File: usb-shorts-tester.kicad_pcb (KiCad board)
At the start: 2 copper layers, 21 x 51 mm, 7 parts, among them J1 CX60-24S-UNIT, J2 USB4080-03-A_REVA1, U1 TCA6424ARGJR

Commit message: Beta release
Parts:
- added C1: 0.1uF, Capacitor_SMD:C_0603_1608Metric, F.Cu at (50.3, 49.4)
- added JP1: I2C0_I2C1_SDA_JMP_Bridged_12, Jumper:SolderJumper-3_P1.3mm_Bridged12_RoundedPad1.0x1.5mm, F.Cu at (48.6, 55.9)
- added JP2: I2C0_I2C1_SCL_JMP_Bridged_12, Jumper:SolderJumper-3_P1.3mm_Bridged12_RoundedPad1.0x1.5mm, F.Cu at (43.6, 55.9)
- added JP5: JMP_ADDR, Jumper:SolderJumper-2_P1.3mm_Open_RoundedPad1.0x1.5mm, F.Cu at (41.0, 50.2)
- added JP6: I2C_PULLUP_JMP_CLOSED, Jumper:SolderJumper-3_P1.3mm_Bridged12_RoundedPad1.0x1.5mm, F.Cu at (46.1, 53.2)
- added R1: 4k7, Resistor_SMD:R_0603_1608Metric, F.Cu at (42.3, 53.7)
- added R2: 4k7, Resistor_SMD:R_0603_1608Metric, F.Cu at (50.0, 53.7)
- added R3: 10k, Resistor_SMD:R_0603_1608Metric, F.Cu at (43.1, 49.2)
- added R4: 10k, Resistor_SMD:R_0603_1608Metric, F.Cu at (48.5, 49.3)
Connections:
- A1 pad 10: unconnected-(A1-GPIO7-Pad10) -> GPIO7
- A1 pad 26: unconnected-(A1-GPIO20-Pad26) -> GPIO20
- A1 pad 27: unconnected-(A1-GPIO21-Pad27) -> GPIO21
- A1 pad 9: unconnected-(A1-GPIO6-Pad9) -> GPIO6
- U1 pad 26: unconnected-(U1-ADDR-Pad26) -> ADDR
- U1 pad 29: unconnected-(U1-SCL-Pad29) -> SCL
- U1 pad 30: unconnected-(U1-SDA-Pad30) -> SDA
- U1 pad 32: unconnected-(U1-~{INT}-Pad32) -> Net-(U1-~{INT})
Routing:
- net GPIO6: track 0.00 -> 29.3 mm, vias 0 -> 2
- net GPIO7: track 0.00 -> 16.9 mm, vias 0 -> 2
- net GND: track 1.91 -> 17.5 mm, vias 0 -> 1
- net GPIO21: track 0.00 -> 14.4 mm, vias 0 -> 1
- net +3V3: track 36.2 -> 50.3 mm, vias 2 -> 5
- net SDA: track 0.00 -> 14.0 mm
- net SCL: track 0.00 -> 12.8 mm
- net RESET: track 11.5 -> 20.2 mm, vias 0 -> 3
- net ADDR: track 0.00 -> 6.15 mm
- net GPIO20: track 0.00 -> 4.86 mm
- net Net-(JP6-B): track 0.00 -> 1.98 mm
- net Net-(JP6-A): track 0.00 -> 1.96 mm
- net Net-(U1-~{INT}): track 0.00 -> 1.86 mm
- net A12: track 46.7 -> 48.2 mm
- net A10: track 46.7 -> 48.0 mm
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
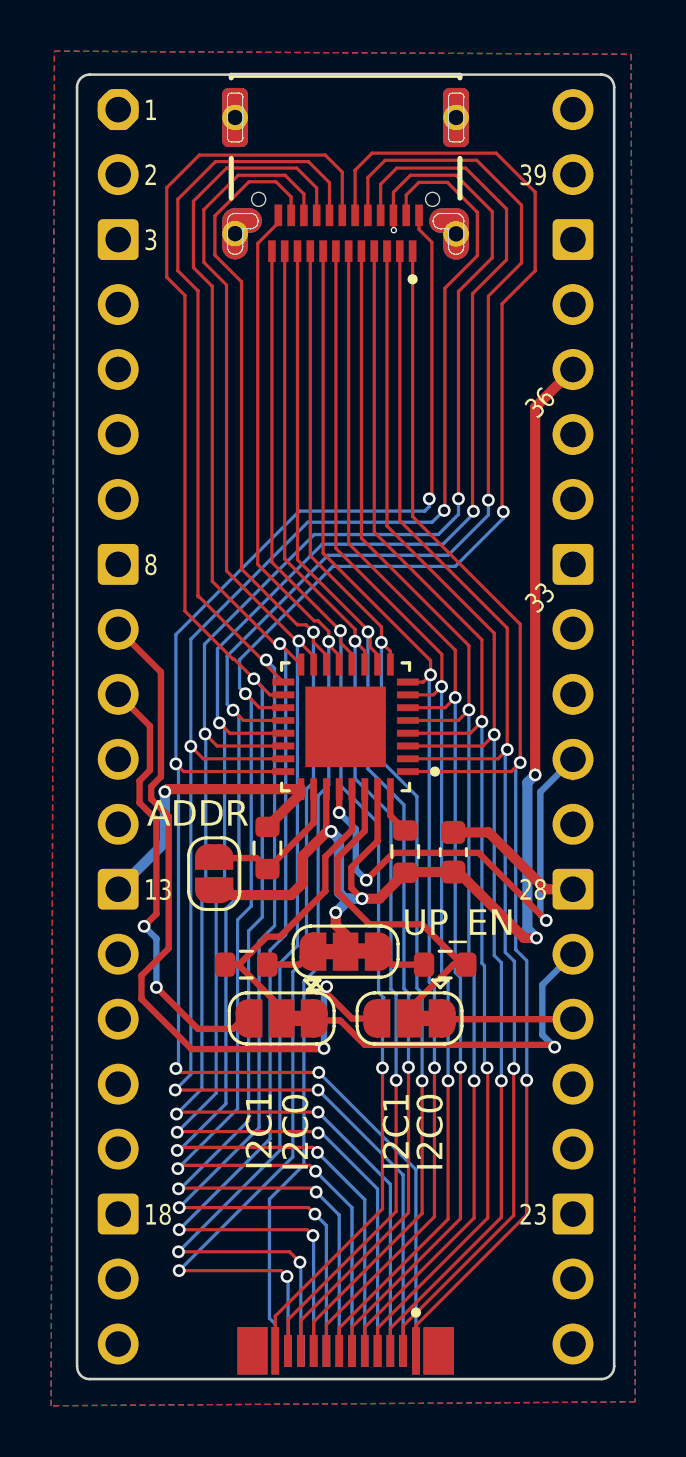
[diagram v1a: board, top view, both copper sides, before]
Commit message: Add usb shield probing
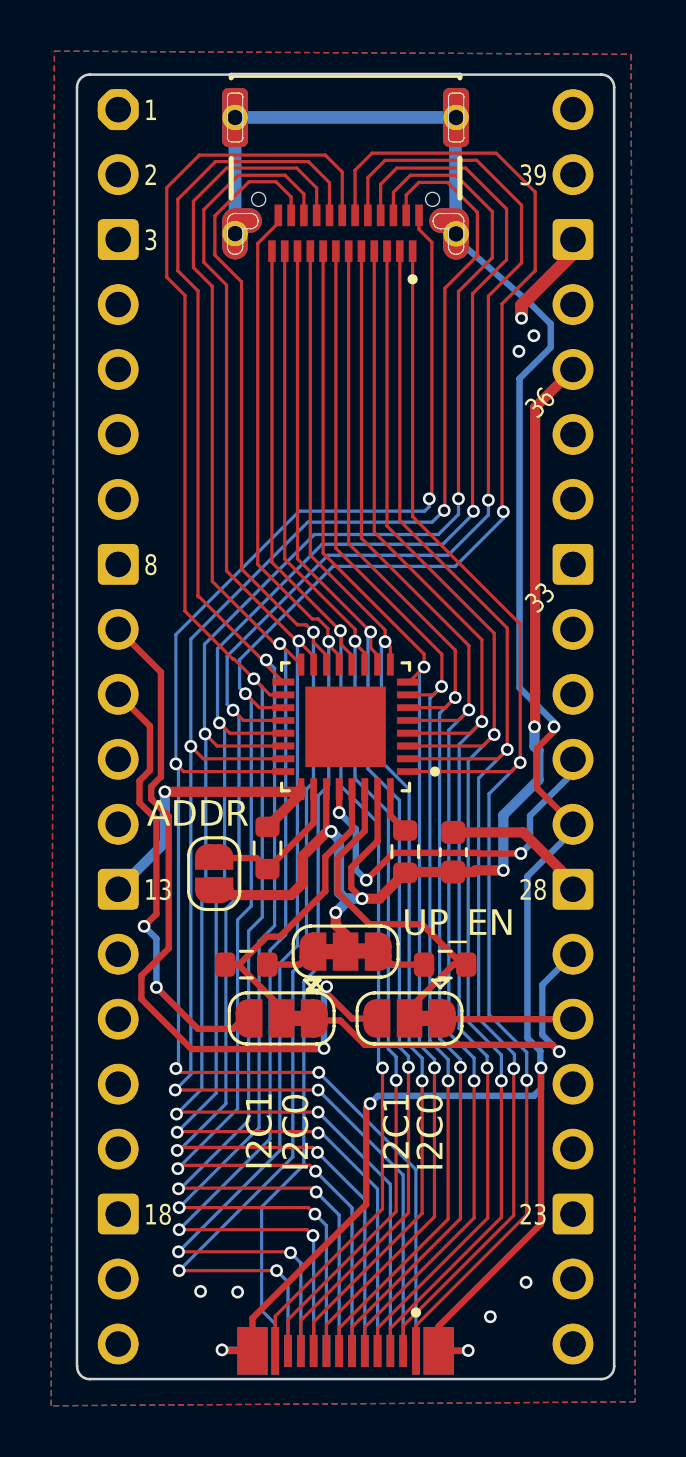
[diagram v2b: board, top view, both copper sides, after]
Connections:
- A1 pad 29: unconnected-(A1-GPIO22-Pad29) -> SHIELD
- J1 pad S1: unconnected-(J1-SHIELD1-PadS1) -> SHIELD
- J1 pad S2: unconnected-(J1-SHIELD1-PadS2) -> SHIELD
- J1 pad S3: unconnected-(J1-SHIELD2-PadS3) -> SHIELD
- J1 pad S4: unconnected-(J1-SHIELD2-PadS4) -> SHIELD
- J2 pad G1: unconnected-(J2-SHIELD-PadG1) -> SHIELD
- J2 pad G2: unconnected-(J2-SHIELD-PadG1) -> SHIELD
- J2 pad G3: unconnected-(J2-SHIELD-PadG1) -> SHIELD
- J2 pad G4: unconnected-(J2-SHIELD-PadG1) -> SHIELD
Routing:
- net SHIELD: track 0.00 -> 70.0 mm, vias 0 -> 5
- net +3V3: track 50.3 -> 45.7 mm
- net RESET: track 20.2 -> 15.7 mm
- net GND: track 17.5 -> 21.6 mm, vias 1 -> 8
- net A2: track 50.8 -> 51.6 mm
- net A1: track 51.3 -> 52.2 mm
- net A3: track 50.2 -> 51.0 mm
- net A4: track 49.7 -> 50.4 mm
- net A5: track 49.1 -> 49.8 mm
- net B10: track 68.8 -> 68.2 mm, vias 5 -> 4
- net A6: track 48.6 -> 49.1 mm
- net GPIO21: track 14.4 -> 14.9 mm

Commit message: Add pulldowns on all expander pins
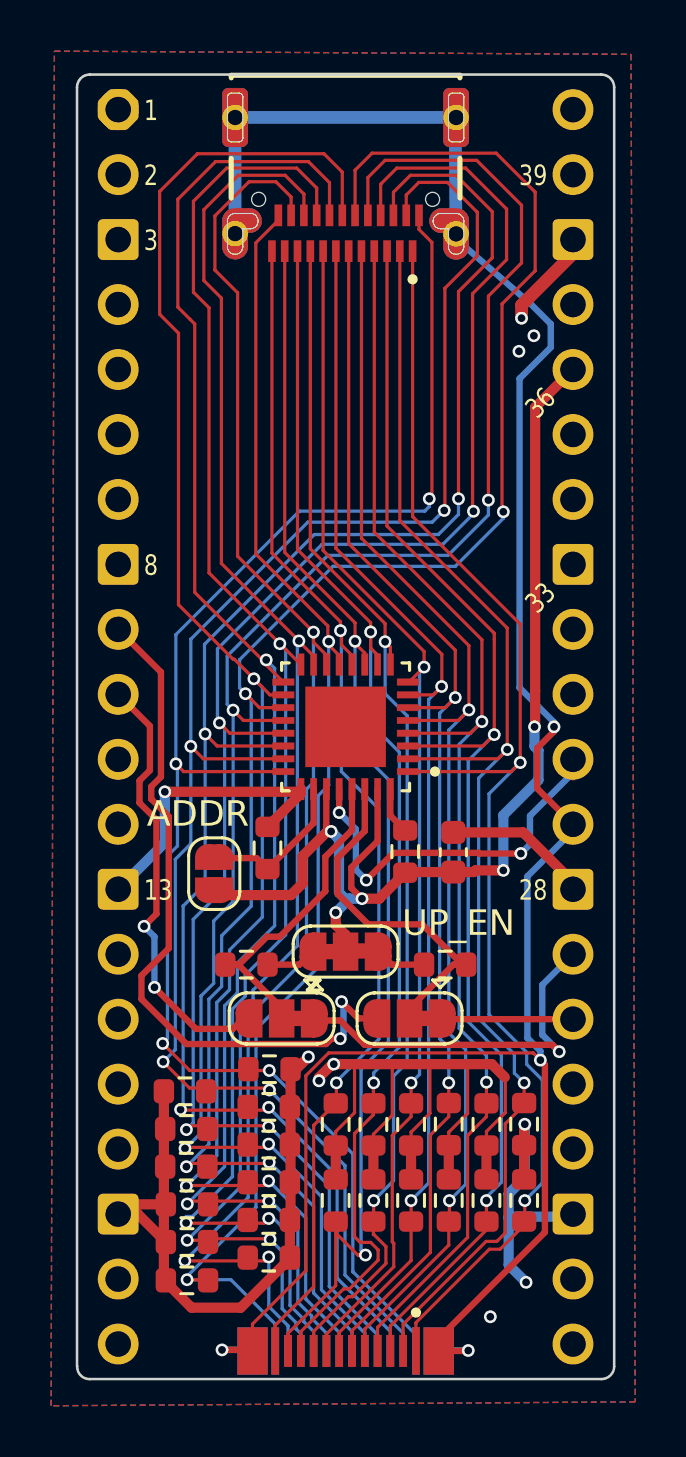
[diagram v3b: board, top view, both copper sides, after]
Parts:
- added R29: 10k, Resistor_SMD:R_0603_1608Metric, F.Cu at (45.7, 63.0)
- added R30: 10k, Resistor_SMD:R_0603_1608Metric, F.Cu at (50.2, 60.0)
- added R31: 10k, Resistor_SMD:R_0603_1608Metric, F.Cu at (45.7, 60.0)
- added R32: 10k, Resistor_SMD:R_0603_1608Metric, F.Cu at (47.2, 60.0)
- added R33: 10k, Resistor_SMD:R_0603_1608Metric, F.Cu at (48.7, 60.0)
- added R34: 10k, Resistor_SMD:R_0603_1608Metric, F.Cu at (51.6, 60.0)
- added R35: 10k, Resistor_SMD:R_0603_1608Metric, F.Cu at (53.1, 60.0)
- added R36: 10k, Resistor_SMD:R_0603_1608Metric, F.Cu at (47.2, 63.0)
- added R37: 10k, Resistor_SMD:R_0603_1608Metric, F.Cu at (48.7, 63.0)
- added R38: 10k, Resistor_SMD:R_0603_1608Metric, F.Cu at (50.2, 63.0)
- added R39: 10k, Resistor_SMD:R_0603_1608Metric, F.Cu at (51.6, 63.0)
- added R40: 10k, Resistor_SMD:R_0603_1608Metric, F.Cu at (53.1, 63.0)
- added R41: 10k, Resistor_SMD:R_0603_1608Metric, F.Cu at (43.2, 57.8)
- added R42: 10k, Resistor_SMD:R_0603_1608Metric, F.Cu at (43.1, 59.3)
- added R43: 10k, Resistor_SMD:R_0603_1608Metric, F.Cu at (43.1, 60.8)
- added R44: 10k, Resistor_SMD:R_0603_1608Metric, F.Cu at (43.1, 62.3)
- added R45: 10k, Resistor_SMD:R_0603_1608Metric, F.Cu at (43.1, 63.7)
- added R46: 10k, Resistor_SMD:R_0603_1608Metric, F.Cu at (43.1, 65.2)
- added R47: 10k, Resistor_SMD:R_0603_1608Metric, F.Cu at (39.9, 58.7)
- added R48: 10k, Resistor_SMD:R_0603_1608Metric, F.Cu at (39.9, 60.2)
- added R49: 10k, Resistor_SMD:R_0603_1608Metric, F.Cu at (39.9, 61.6)
- added R50: 10k, Resistor_SMD:R_0603_1608Metric, F.Cu at (39.9, 63.1)
- added R51: 10k, Resistor_SMD:R_0603_1608Metric, F.Cu at (39.9, 64.6)
- added R52: 10k, Resistor_SMD:R_0603_1608Metric, F.Cu at (39.9, 66.1)
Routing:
- net GND: track 21.6 -> 90.6 mm, vias 8 -> 10
- net B1: track 48.4 -> 52.7 mm, vias 1 -> 2
- net A11: track 47.6 -> 50.3 mm
- net SHIELD: track 70.0 -> 72.0 mm, vias 5 -> 4
- net B8: track 70.5 -> 68.9 mm
- net B9: track 69.3 -> 67.8 mm
- net B7: track 71.8 -> 70.4 mm
- net B10: track 68.2 -> 66.9 mm
- net GPIO6: track 29.3 -> 28.0 mm
- net A7: track 48.4 -> 47.2 mm
- net B5: track 62.9 -> 61.7 mm
- net B11: track 67.3 -> 66.2 mm
- net B12: track 63.1 -> 62.2 mm
- net B6: track 64.9 -> 64.1 mm
- net B4: track 61.3 -> 60.4 mm
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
